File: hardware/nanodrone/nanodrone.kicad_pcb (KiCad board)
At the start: 4 copper layers, 50.8 x 22.9 mm, 22 parts, among them J1 RTR0, J2 RTR1, J3 RTR2, J4 RTR3, Q1 2N7002, Q2 2N7002, Q3 2N7002, Q4 2N7002, U1 Feather

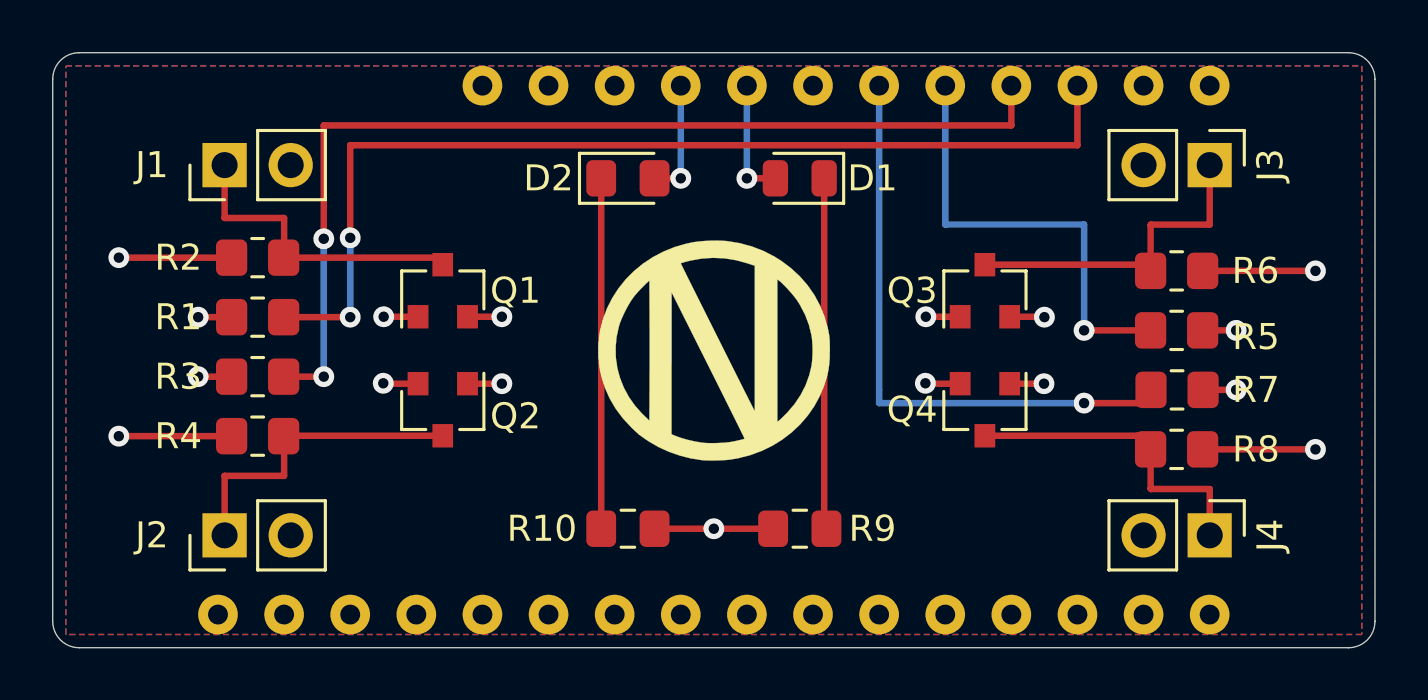
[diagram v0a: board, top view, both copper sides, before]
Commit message: Fix pwm connection. Add jlcpcb part numbers
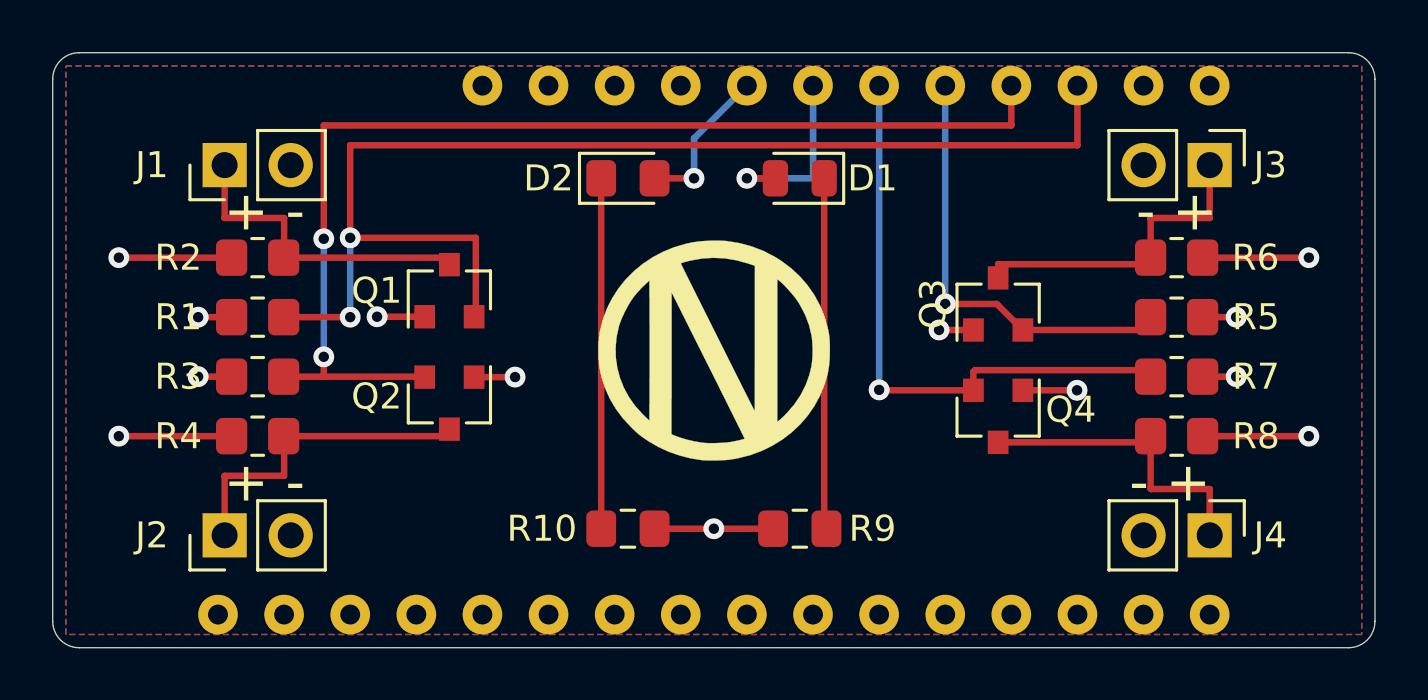
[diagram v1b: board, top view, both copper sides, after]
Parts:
- D1: value DGB0 -> DGB1
- D2: value DBG1 -> DBG2
- Q1, Q2, Q3, Q4: value 2N7002 -> NUD3124LT1G
- moved Q3 0.72 mm to (154.2, 94.2)
- moved Q4 0.57 mm to (154.2, 98.6)
- moved R7 0.51 mm to (161.0, 97.0)
- moved R8 0.51 mm to (161.0, 99.3)
- moved R5 0.51 mm to (161.0, 94.7)
- moved R6 0.51 mm to (161.0, 92.5)
- moved Q2 0.36 mm to (133.1, 98.0)
- moved Q1 0.25 mm to (133.1, 93.7)
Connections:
- D1 pad 2: /dgb0 -> /dbg1
- D2 pad 2: /dgb1 -> /dbg2
- Q1 pad 2: GND -> /rtrctl0
- Q2 pad 2: GND -> /rtrctl1
- Q3 pad 2: GND -> /rtrctl2
- Q4 pad 2: GND -> /rtrctl3
- U1 pad 4: /dgb1 -> Net-(U1-Pad4)
- U1 pad 5: /dgb0 -> /dbg2
- U1 pad 6: Net-(U1-Pad6) -> /dbg1
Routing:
- net /rtrctl0: track 39.4 -> 47.3 mm
- net /dbg1: track 0.00 -> 7.19 mm, vias 0 -> 1
- net /dbg2: track 0.00 -> 5.92 mm, vias 0 -> 1
- net GND: track 9.90 -> 4.55 mm, vias 5 -> 1
- net /dgb0: track 4.65 -> 0.00 mm, vias 1 -> 0
- net /dgb1: track 4.57 -> 0.00 mm, vias 1 -> 0
- net /rtrctl1: track 39.6 -> 43.5 mm
- net +3V3: track 10.4 -> 11.9 mm
- net +BATT: track 17.3 -> 16.8 mm
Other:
- board text added: "+ -"
- board text added: "- +"
- board text added: "nanodrone :: RevB nnarain"
- board text removed: "nanodrone :: RevA nnarain"
